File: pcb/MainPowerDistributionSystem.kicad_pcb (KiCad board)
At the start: 2 copper layers, 66 x 60 mm, 36 parts, among them J2 PREC040DBAN-M71RC, Q1 S8050, U1 D24V7F3, U2 D24V7F3, U3 D24V7F3, U4 BTS462TATMA1, U5 LM339, U8 BTS462TATMA1

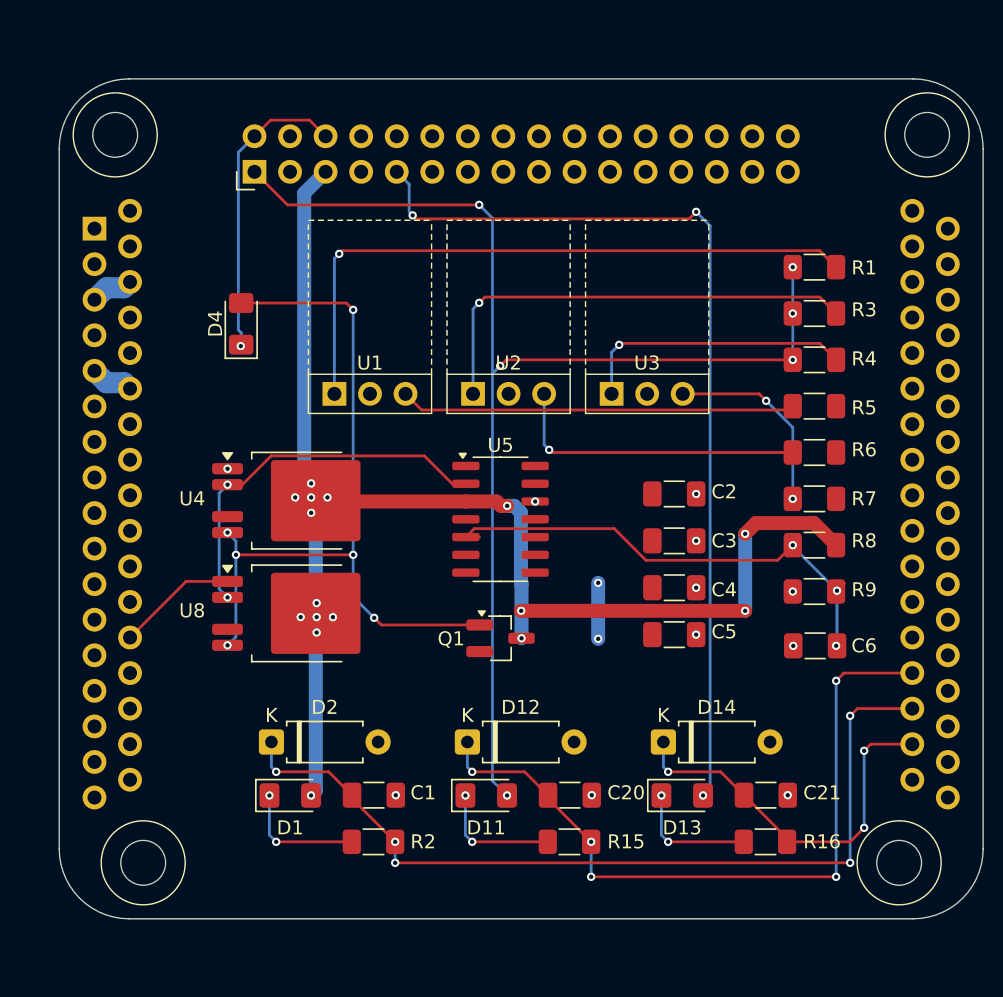
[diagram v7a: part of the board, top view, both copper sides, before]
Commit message: Mostly finalized `MainPowerDistributionSystem`.
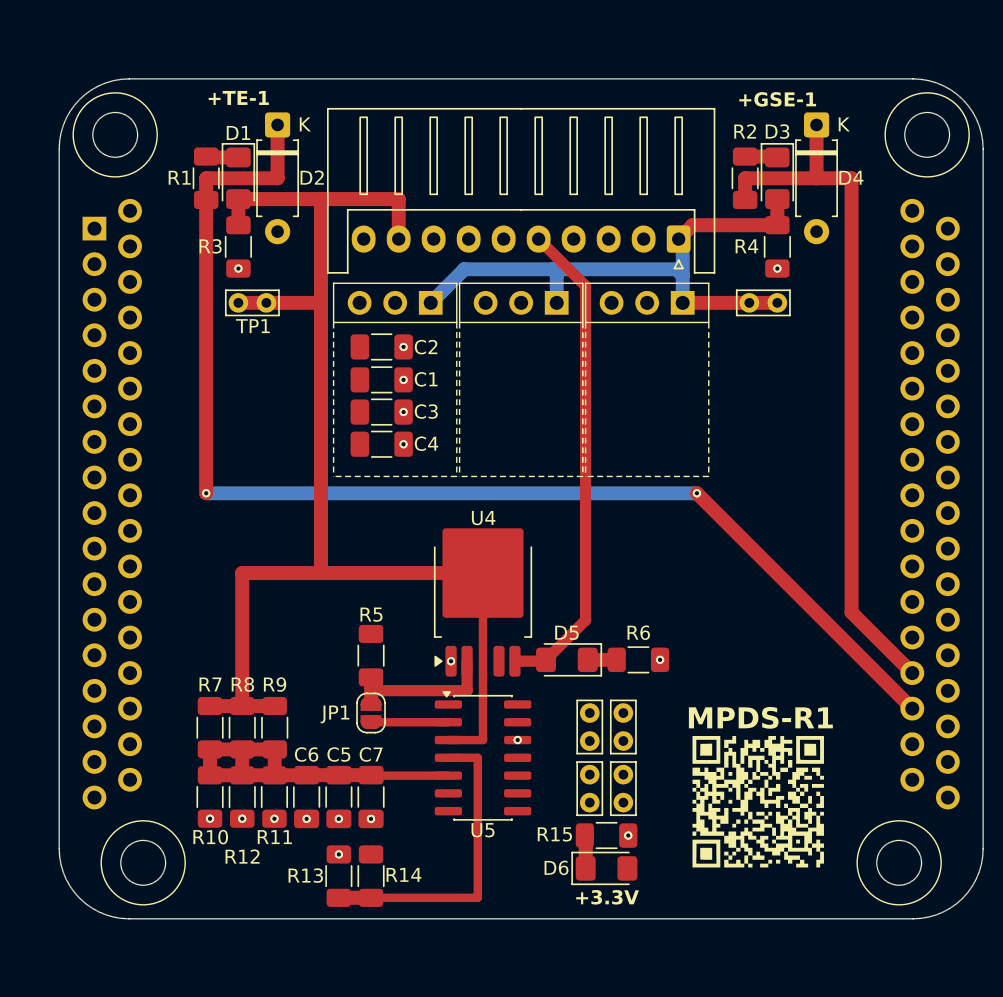
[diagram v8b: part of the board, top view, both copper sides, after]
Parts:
- removed the C1 at (139.5, 121.2)
- removed C20, C21: 1u, Capacitor_SMD:C_1206_3216Metric_Pad1.33x1.80mm_HandSolder
- removed D13: WHITE, LED_SMD:LED_1206_3216Metric_Pad1.42x1.75mm_HandSolder
- removed D14: 1N4727A, Diode_THT:D_A-405_P7.62mm_Horizontal
- removed the D4 at (130.0, 87.5)
- removed Q1: S8050, Package_TO_SOT_SMD:SOT-23_Handsoldering
- removed the R1 at (170.9, 83.5)
- removed R16: 3k, Resistor_SMD:R_1206_3216Metric_Pad1.30x1.75mm_HandSolder
- removed the R7 at (170.9, 100.0)
- removed the U4 at (134.1, 100.1)
- added C5: ?, Capacitor_SMD:C_1206_3216Metric_Pad1.33x1.80mm_HandSolder, F.Cu at (137.0, 121.3)
- added C7: ?, Capacitor_SMD:C_1206_3216Metric_Pad1.33x1.80mm_HandSolder, F.Cu at (139.3, 121.3)
- added D5: RED, LED_SMD:LED_1206_3216Metric_Pad1.42x1.75mm_HandSolder, F.Cu at (153.3, 111.5)
- added D6: GREEN, LED_SMD:LED_1206_3216Metric_Pad1.42x1.75mm_HandSolder, F.Cu at (156.1, 126.4)
- added G***: LOGO, LOGO, F.Cu at (166.9, 121.6)
- added G***: LOGO, LOGO, B.Cu at (150.1, 104.1)
- added JP1: SolderJumper_2_Open, Jumper:SolderJumper-2_P1.3mm_Open_RoundedPad1.0x1.5mm, F.Cu at (139.3, 115.3)
- added R10: 360k, Resistor_SMD:R_1206_3216Metric_Pad1.30x1.75mm_HandSolder, F.Cu at (127.8, 121.3)
- added R11: ?, Resistor_SMD:R_1206_3216Metric_Pad1.30x1.75mm_HandSolder, F.Cu at (132.4, 121.3)
- added R12: ?, Resistor_SMD:R_1206_3216Metric_Pad1.30x1.75mm_HandSolder, F.Cu at (130.1, 121.3)
- added R13: ?, Resistor_SMD:R_1206_3216Metric_Pad1.30x1.75mm_HandSolder, F.Cu at (137.0, 126.9)
- added R14: 0, Resistor_SMD:R_1206_3216Metric_Pad1.30x1.75mm_HandSolder, F.Cu at (139.3, 126.9)
- added R15: 10k, Resistor_SMD:R_1206_3216Metric_Pad1.30x1.75mm_HandSolder, F.Cu at (156.1, 124.0)
- added R8: ?, Resistor_SMD:R_1206_3216Metric_Pad1.30x1.75mm_HandSolder, F.Cu at (130.1, 116.4)
- added TP1: TestPoint, TestPoint:TestPoint_Bridge_Pitch2.0mm_Drill0.7mm, F.Cu at (129.8, 86.0)
- added TP2: TestPoint, TestPoint:TestPoint_Bridge_Pitch2.0mm_Drill0.7mm, F.Cu at (166.3, 86.0)
- added TP3: TestPoint, TestPoint:TestPoint_Bridge_Pitch2.0mm_Drill0.7mm, F.Cu at (157.3, 117.3)
- added TP4: TestPoint, TestPoint:TestPoint_Bridge_Pitch2.0mm_Drill0.7mm, F.Cu at (154.9, 117.3)
- added TP5: TestPoint, TestPoint:TestPoint_Bridge_Pitch2.0mm_Drill0.7mm, F.Cu at (154.9, 121.7)
- added TP6: TestPoint, TestPoint:TestPoint_Bridge_Pitch2.0mm_Drill0.7mm, F.Cu at (157.3, 121.7)
- J1: value ~ -> Conn_02x05_Top_Bottom; footprint pcb:MainStackConnector -> Connector_JST:JST_XH_S10B-XH-A_1x10_P2.50mm_Horizontal
- J2: value PREC040DBAN-M71RC -> ~; footprint pcb:PinHeader_2x16_P2.54mm_Horizontal_SmallSilkscreen -> pcb:MainStackConnector
- N1: footprint pcb:Dummy -> pcb:MainPowerDistributionSystemHousing
- R3, R4, R5, R6: value 0 -> 100k
- R9: value 360k -> ?
- moved D4 50.6 mm to (171.1, 73.3), turned to -90 degrees
- moved R2 49.0 mm to (166.0, 77.1), turned to -90 degrees
- moved R1 48.9 mm to (127.5, 77.1), turned to -90 degrees
- moved D3 48.7 mm to (168.3, 77.1), turned to -90 degrees
- moved R7 45.1 mm to (127.8, 116.4), turned to 90 degrees
- moved D1 44.2 mm to (129.8, 77.1), turned to -90 degrees
- moved D2 44.1 mm to (132.6, 73.3), turned to -90 degrees
- moved R3 41.4 mm to (129.8, 82.0), turned to -90 degrees
- moved R9 39.8 mm to (132.4, 116.4), turned to 90 degrees
- moved C6 37.9 mm to (134.7, 121.3), turned to -90 degrees
- moved R5 36.3 mm to (139.3, 111.2), turned to 90 degrees
- moved J2 30.1 mm to (150.0, 100.0), turned to 0 degrees
- moved C4 24.9 mm to (140.0, 96.1)
- moved C3 24.4 mm to (140.0, 93.8)
- moved C1 23.9 mm to (140.0, 91.5)
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- renumbered C3 to C1, C4 to C3, C5 to C4, D11 to D3, D12 to D4, R2 to R1, R15 to R2, R8 to R7, U8 to U4
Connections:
- D2 pad 1: LOGIC_TIMER_EVENT_1 -> logic_timer_event_1
- D4 pad 1: LOGIC_GSE_1 -> logic_gse_1
- J1 pad 1: +3.3V -> +GSE-1
- J1 pad 2: unconnected-(J1-spi_clock_A-Pad2) -> GND
- J1 pad 3: GND -> +3.3V
- J1 pad 4: unconnected-(J1-spi_mosi_A-Pad4) -> GND
- J1 pad 5: GND -> BURNWIRE_VOLTAGE
- J1 pad 6: unconnected-(J1-spi_miso_A-Pad6) -> GND
- J1 pad 8: unconnected-(J1-spi_nss_A-Pad8) -> GND
- J1 pad 9: unconnected-(J1-spi_ready_A-Pad9) -> +TE-1
- J2 pad 1: +GSE-1 -> +3.3V
- J2 pad 10: unconnected-(J2-Pin_10-Pad10) -> GND
- J2 pad 11: GND -> +3.3V
- J2 pad 13: +3.3V -> unconnected-(J2-uart_rx_A-Pad13)
- J2 pad 14: unconnected-(J2-Pin_14-Pad14) -> GND
- J2 pad 15: GND -> unconnected-(J2-general_purpose_A-Pad15)
- J2 pad 19: GND -> unconnected-(J2-i2c_data_A-Pad19)
- J2 pad 2: BURNWIRE_VOLTAGE -> unconnected-(J2-spi_clock_A-Pad2)
- J2 pad 20: unconnected-(J2-Pin_20-Pad20) -> GND
- J2 pad 25: +3.3V -> GND
- J2 pad 27: GND -> +3.3V
- J2 pad 30: unconnected-(J2-Pin_30-Pad30) -> GND
- J2 pad 31: unconnected-(J2-Pin_31-Pad31) -> +3.3V
- J2 pad 4: GND -> unconnected-(J2-spi_mosi_A-Pad4)
- J2 pad 5: +TE-1 -> GND
- J2 pad 6: BURNWIRE_VOLTAGE -> unconnected-(J2-spi_miso_A-Pad6)
- J2 pad 7: GND -> +3.3V
- J2 pad 8: GND -> unconnected-(J2-spi_nss_A-Pad8)
- J2 pad 9: +TE-X -> unconnected-(J2-spi_ready_A-Pad9)
- R1 pad 2: LOGIC_TIMER_EVENT_1 -> logic_timer_event_1
- R2 pad 2: LOGIC_GSE_1 -> logic_gse_1
- R3 pad 1: +GSE-1 -> +TE-1
- R3 pad 2: Net-(R3-Pad2) -> GND
- R4 pad 2: Net-(R4-Pad2) -> GND
- R5 pad 1: Net-(R5-Pad1) -> Net-(JP1-B)
- R6 pad 1: Net-(R6-Pad1) -> Net-(D5-K)
- R6 pad 2: +3.3V -> GND
- R9 pad 1: GND -> Net-(U5A-+)
- R9 pad 2: Net-(U5A-+) -> +TE-1
- U1 pad VIN: Net-(R1-Pad2) -> +GSE-1
- U1 pad VOUT: Net-(R5-Pad1) -> +3.3V
- U2 pad VIN: Net-(R3-Pad2) -> +GSE-1
- U2 pad VOUT: Net-(R6-Pad1) -> +3.3V
- U3 pad VIN: Net-(R4-Pad2) -> +GSE-1
- U3 pad VOUT: Net-(R7-Pad1) -> +3.3V
- U4 pad 2: Net-(U4-IN) -> Net-(JP1-B)
- U4 pad 5: Net-(D4-A) -> BURNWIRE_VOLTAGE
- U5 pad 2: Net-(U4-IN) -> Net-(JP1-A)
- U5 pad 4: +3.3V -> Net-(U5A--)
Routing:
- net logic_timer_event_1: track 0.00 -> 88.2 mm, vias 0 -> 2
- net +TE-X: track 66.5 -> 0.00 mm, vias 3 -> 0
- net LOGIC_TIMER_EVENT_1: track 62.1 -> 0.00 mm, vias 5 -> 0
- net Net-(D4-A): track 55.5 -> 0.00 mm, vias 6 -> 0
- net LOGIC_GSE_1: track 52.7 -> 0.00 mm, vias 5 -> 0
- net logic_gse_1: track 0.00 -> 50.1 mm
- net Net-(R1-Pad2): track 46.2 -> 0.00 mm, vias 1 -> 0
- net +GSE-1: track 88.5 -> 42.7 mm, vias 6 -> 0
- net Net-(R3-Pad2): track 32.8 -> 0.00 mm, vias 1 -> 0
- net Net-(R5-Pad1): track 28.2 -> 0.00 mm
- net LOGIC_TIMER_EVENT_X: track 28.0 -> 0.00 mm, vias 3 -> 0
- net Net-(U4-IN): track 27.3 -> 0.00 mm, vias 2 -> 0
- net +TE-1: track 116.7 -> 94.5 mm, vias 16 -> 0
- net Net-(U5A--): track 0.00 -> 22.0 mm
- net Net-(R6-Pad1): track 21.6 -> 0.00 mm, vias 1 -> 0
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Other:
- board text added: "+3.3V"
- board text added: "+GSE-1"
- board text added: "+TE-1"
- board text added: "MPDS-R1"
